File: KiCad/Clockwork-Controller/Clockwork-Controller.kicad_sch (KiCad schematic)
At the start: 99 parts, among them CN2 PJ-307N5, J1 DIN-6 male, J2 to DIN-6 Male, J3 Pause Button, J4 ICSP, J5 LED-Connector, J6 FTDI, Q1 AO3400A, Q2 SS8050, Q3 SS8050, Q4 SS8050, SW1 Guide/Follow, SW2 Mode -, SW3 Mode +, SW4 Frame -, SW5 Frame +, U1 ECS-TXO-3225MV-160-TR, U2 AP2210N-3.3TRG1, U3 74HCT14, U4 G3VM-61VY3(TR), U5 MCP4725, U6 LMC6482, U7 ATmega328P-A

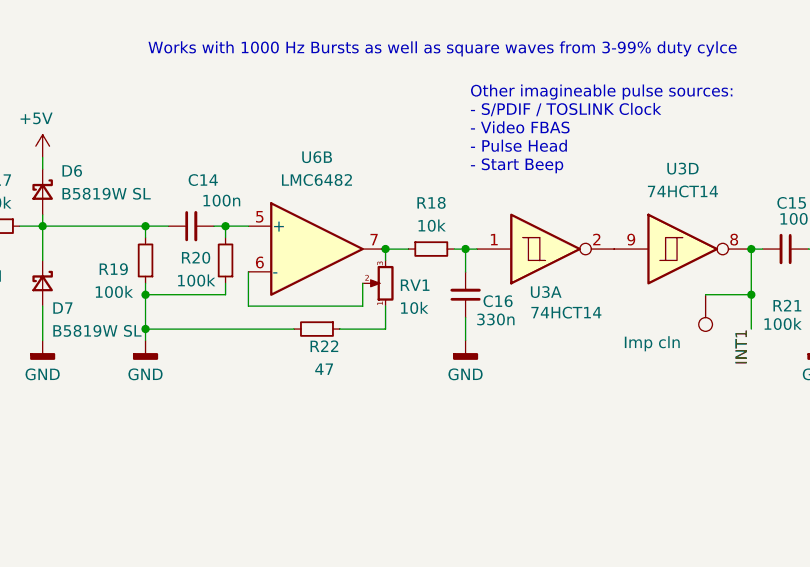
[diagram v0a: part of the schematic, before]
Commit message: Potentiometer Flip for more intuitive Pulse Amp control
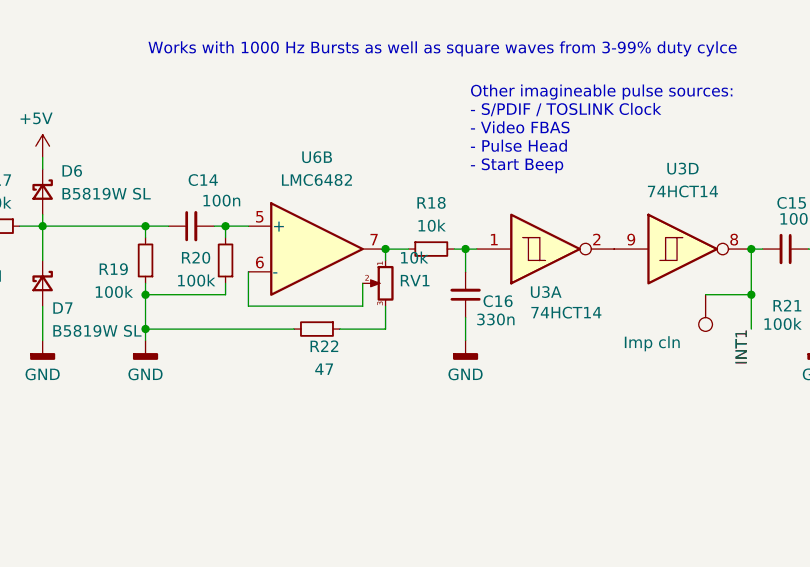
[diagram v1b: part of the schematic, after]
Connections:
- net at RV1.1: now also R18.1, U6.7; no longer R22.1
- new net: R22.1, RV1.3
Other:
- moved on the sheet: RV1
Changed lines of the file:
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@@
 	(symbol
 		(lib_id "Device:R_Potentiometer_Small")
-		(at 259.08 190.5 180)
+		(at 259.08 190.5 0)
+		(mirror y)
 		(unit 1)
 		(exclude_from_sim no)
@@
 		(dnp no)
 		(property "Reference" "RV1"
-			(at 260.604 190.754 0)
+			(at 260.604 190.246 0)
 			(effects
 				(font
@@
 		)
 		(property "Value" "10k"
-			(at 260.604 193.294 0)
+			(at 260.604 187.706 0)
 			(effects
 				(font

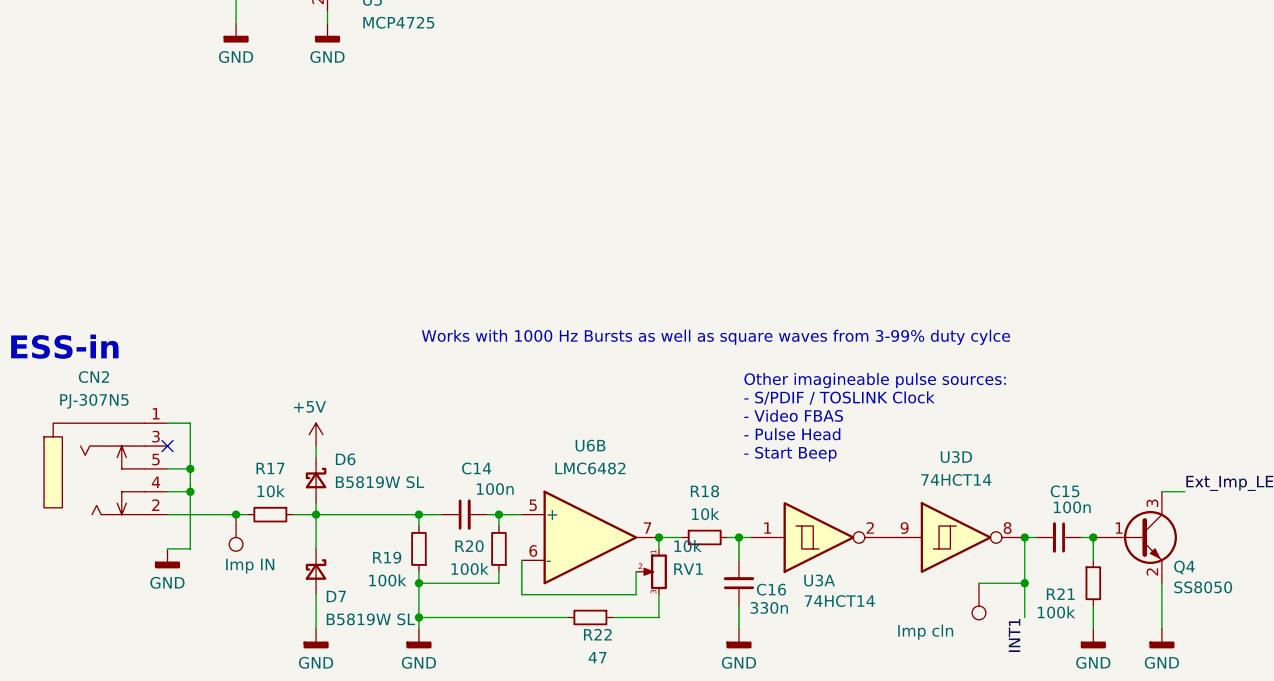
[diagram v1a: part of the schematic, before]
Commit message: Using both left and right channel for ESS in
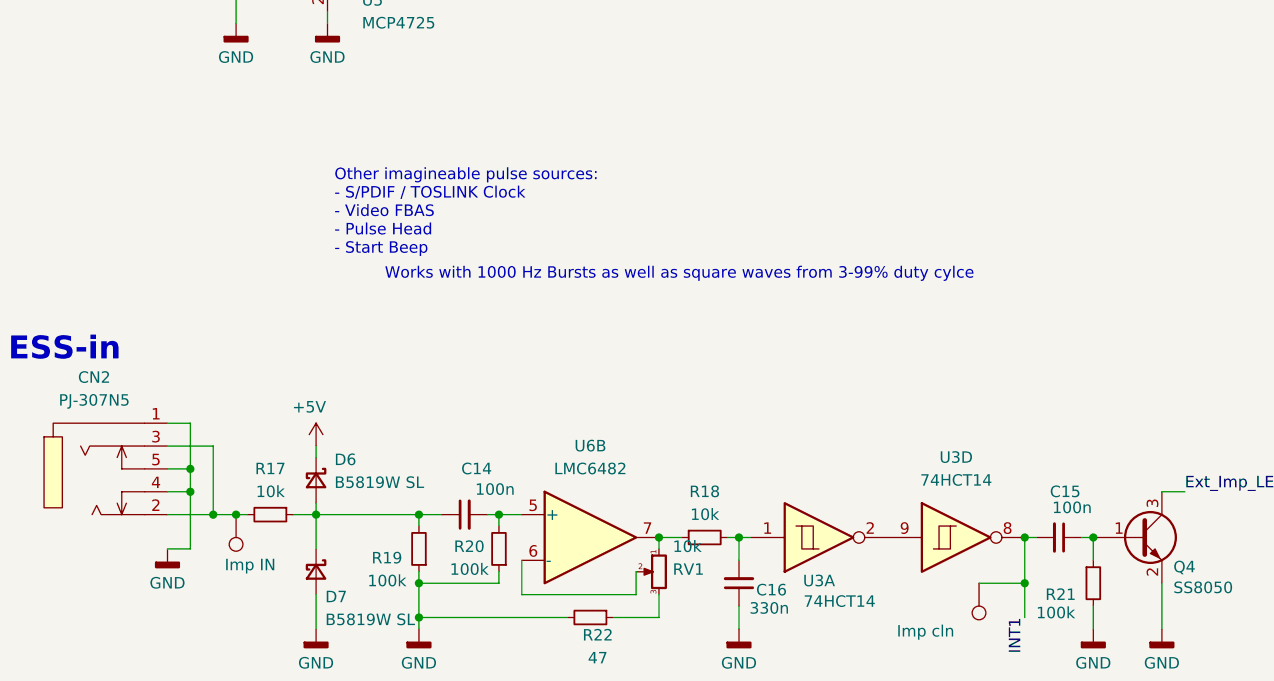
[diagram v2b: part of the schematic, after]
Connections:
- net at CN2.2, R17.2, TP9.1: now also CN2.3
- no-connect marks 2 -> 1
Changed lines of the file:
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@@
+	)
+	(junction
+		(at 209.55 184.15)
+		(diameter 0)
+		(color 0 0 0 0)
 	)
 	(junction
@@
 		(at 78.74 194.31)
 	)
-	(no_connect
-		(at 204.47 176.53)
-	)
 	(wire
 		(pts
@@
 	(wire
 		(pts
+			(xy 204.47 176.53) (xy 209.55 176.53)
+		)
+		(stroke
+			(width 0)
+			(type default)
+		)
+	)
+	(wire
+		(pts
 			(xy 306.07 186.69) (xy 307.34 186.69)
 		)
@@
 	(wire
 		(pts
+			(xy 209.55 184.15) (xy 212.09 184.15)
+		)
+		(stroke
+			(width 0)
+			(type default)
+		)
+	)
+	(wire
+		(pts
 			(xy 106.68 214.63) (xy 106.68 219.71)
 		)
@@
 	(wire
 		(pts
-			(xy 204.47 184.15) (xy 212.09 184.15)
+			(xy 204.47 184.15) (xy 209.55 184.15)
 		)
 		(stroke
@@
 		(pts
 			(xy 149.86 60.96) (xy 149.86 58.42)
+		)
+		(stroke
+			(width 0)
+			(type default)
+		)
+	)
+	(wire
+		(pts
+			(xy 209.55 176.53) (xy 209.55 184.15)
 		)
 		(stroke
@@
 	(text "Other imagineable pulse sources:\n- S/PDIF / TOSLINK Clock\n- Video FBAS\n- Pulse Head\n- Start Beep"
 		(exclude_from_sim no)
-		(at 268.478 173.482 0)
+		(at 223.012 150.622 0)
 		(effects
 			(font
@@
 	(text "Works with 1000 Hz Bursts as well as square waves from 3-99% duty cylce"
 		(exclude_from_sim no)
-		(at 265.43 164.592 0)
+		(at 261.366 157.48 0)
 		(effects
 			(font

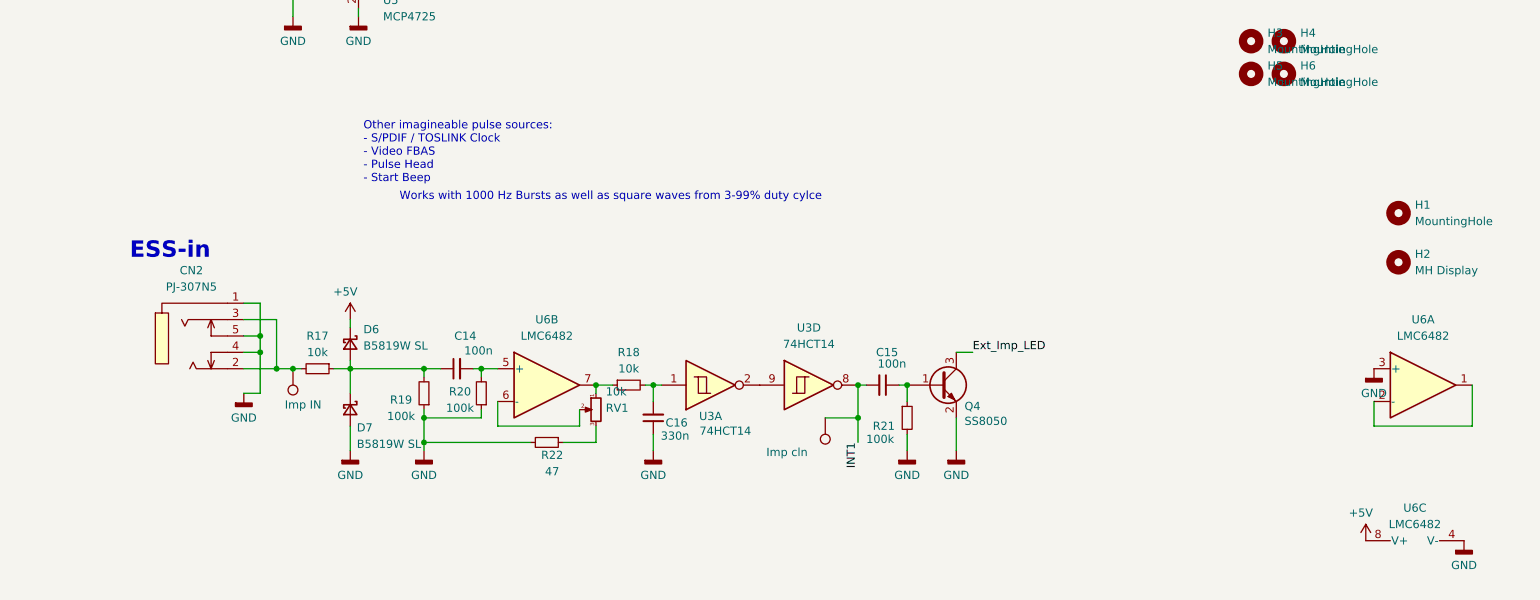
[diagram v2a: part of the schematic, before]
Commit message: Properly summing up R and L channel using the second OpAmp
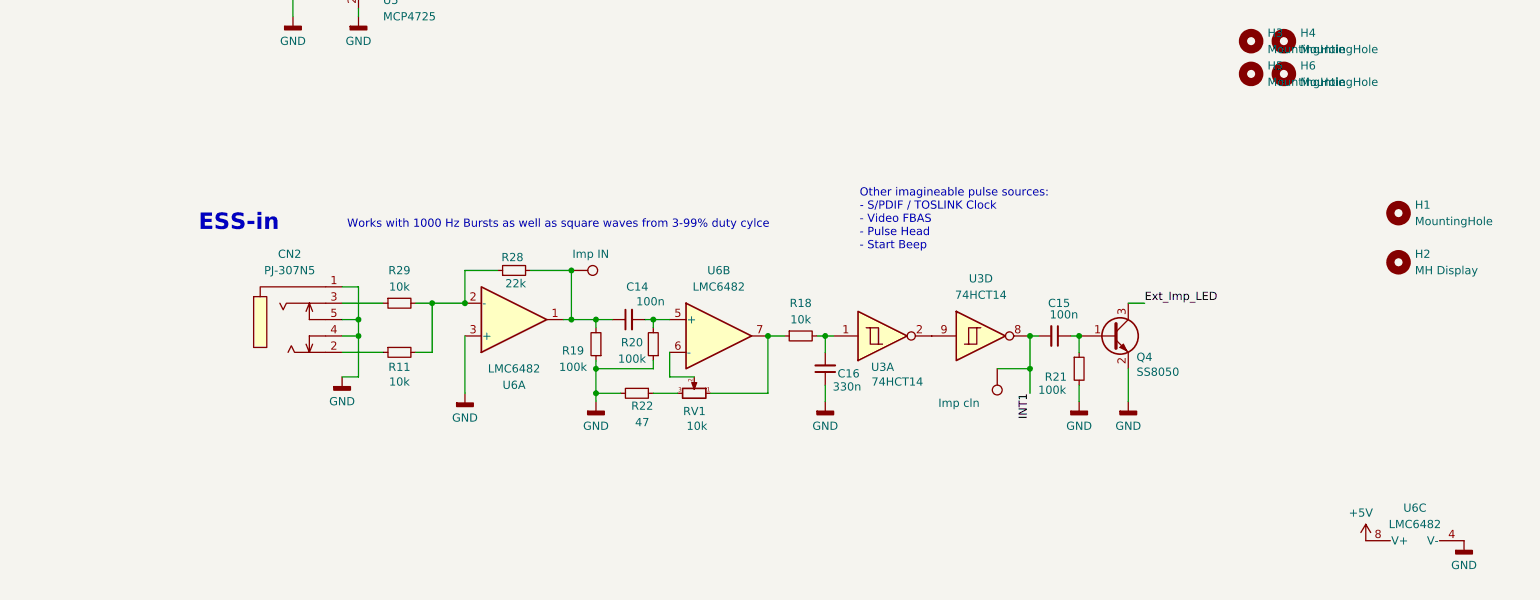
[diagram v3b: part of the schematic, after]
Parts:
- removed D6, D7: B5819W SL, Diode_SMD:D_SOD-123, symbol Device:D_Schottky_Small
- removed R17: 10k, Resistor_SMD:R_0603_1608Metric, symbol Device:R_Small
- added R11, R29: 10k, Resistor_SMD:R_0603_1608Metric, symbol Device:R_Small
- added R28: 22k, Resistor_SMD:R_0603_1608Metric, symbol Device:R_Small
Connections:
- net at C14.1, R19.2: now also TP9.1, U6.1, R28.2
- net at U6.2 (-): now also R11.2, R28.1, R29.2; no longer U6.1
- new net: CN2.2, R11.1
- new net: CN2.3, R29.1
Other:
- moved on the sheet: C14, C15, C16, CN2, Q4, R18, R19, R20, R21, R22, RV1, U3A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
